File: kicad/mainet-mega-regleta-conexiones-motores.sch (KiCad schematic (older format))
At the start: 38 parts, among them J106 Screw_Terminal_01x02, J107 Conn_01x01_Male, J108 Conn_01x01_Male, J109 Conn_01x01_Male, J110 Conn_01x01_Male, J111 Conn_01x01_Male, J112 Conn_01x01_Male, J113 Conn_01x01_Male, J114 Conn_01x01_Male, J115 Conn_01x01_Male, J116 Conn_01x01_Male, J117 Conn_01x01_Male, J118 Conn_01x01_Male, J119 Conn_01x01_Male, J120 Conn_01x01_Male, J121 Conn_01x01_Male, J122 Conn_01x01_Male, J123 Conn_01x01_Male, J124 Conn_01x01_Male, J125 Conn_01x01_Male, J126 Conn_01x01_Male, J127 Conn_01x01_Male, J93 Regleta de Conexiones, J94 Screw_Terminal_01x15, J95 Conn_01x01_Male, J96 Conn_01x01_Male, J97 Conn_01x01_Male, J98 Screw_Terminal_01x02, M1 Upper Clutch, M2 Lower Clutch 1, M3 Lower Clutch 2, M4 Brake, M5 Upper Clutch Fan, M6 Lower Clutch 1 Fan, M7 Lower Clutch 2 Fan, M8 Brake Fan

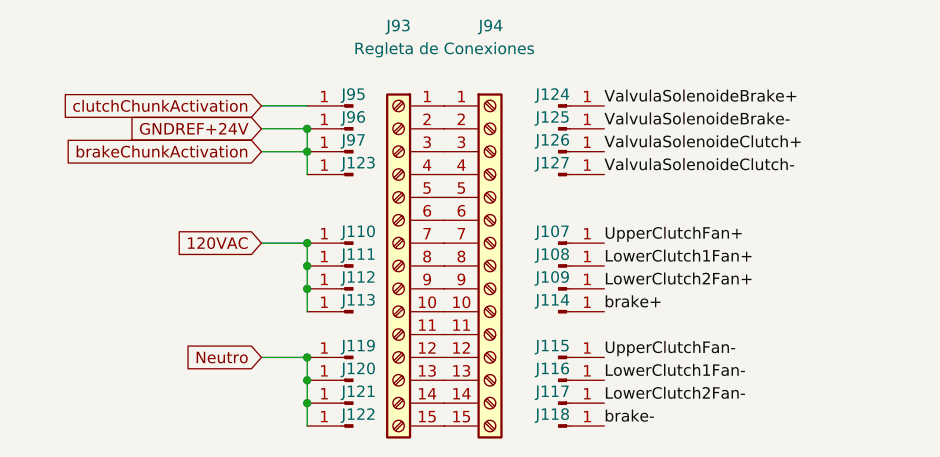
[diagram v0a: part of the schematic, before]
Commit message: KICAD: Agregar conexiones de la Guía de banda regleta de conexiones
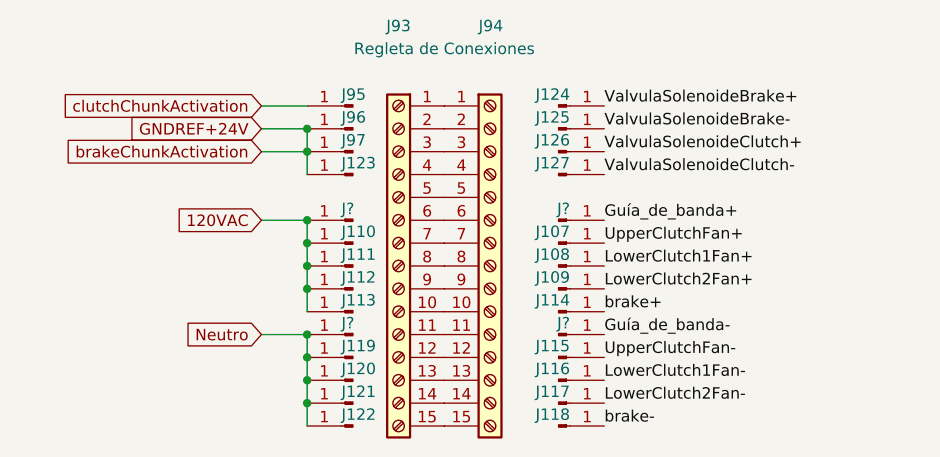
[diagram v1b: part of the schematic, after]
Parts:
- added J? (x4): Conn_01x01_Male, symbol Connector:Conn_01x01_Male
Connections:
- net 120VAC: now also J?.1 (Pin_1)
- net Neutro: now also J?.1 (Pin_1)
- new net Guía_de_banda+: J?.1 (Pin_1)
- new net Guía_de_banda-: J?.1 (Pin_1)
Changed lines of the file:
@@
 Text GLabel 2750 5350 0    50   Input ~ 0
 brakeChunkActivation
-Text GLabel 2750 6250 0    50   Input ~ 0
+Text GLabel 2750 6150 0    50   Input ~ 0
 Neutro
-Text GLabel 2750 5750 0    50   Input ~ 0
+Text GLabel 2750 5650 0    50   Input ~ 0
 120VAC
 $Comp
@@
 	2950 5350 2950 5450
 Wire Wire Line
-	2750 5750 2950 5750
+	2750 5650 2950 5650
 Connection ~ 2950 5750
 Wire Wire Line
-	2750 6250 2950 6250
+	2750 6150 2950 6150
 Connection ~ 2950 6250
 Wire Wire Line
@@
 Text Notes 3350 3500 0    50   ~ 0
 Output-
+$Comp
+L Connector:Conn_01x01_Male J?
+U 1 1 60F7D678
+P 3150 5650
+F 0 "J?" H 3200 5700 50  0000 R CNN
+F 1 "Conn_01x01_Male" H 3122 5583 50  0001 R CNN
+F 2 "" H 3150 5650 50  0001 C CNN
+F 3 "~" H 3150 5650 50  0001 C CNN
+	1    3150 5650
+	-1   0    0    -1
+$EndComp
+$Comp
+L Connector:Conn_01x01_Male J?
+U 1 1 60F7DA90
+P 3150 6150
+F 0 "J?" H 3200 6200 50  0000 R CNN
+F 1 "Conn_01x01_Male" H 3122 6083 50  0001 R CNN
+F 2 "" H 3150 6150 50  0001 C CNN
+F 3 "~" H 3150 6150 50  0001 C CNN
+	1    3150 6150
+	-1   0    0    -1
+$EndComp
+$Comp
+L Connector:Conn_01x01_Male J?
+U 1 1 60F7DEC1
+P 4050 5650
+F 0 "J?" H 4100 5700 50  0000 R CNN
+F 1 "Conn_01x01_Male" H 4022 5583 50  0001 R CNN
+F 2 "" H 4050 5650 50  0001 C CNN
+F 3 "~" H 4050 5650 50  0001 C CNN
+	1    4050 5650
+	1    0    0    -1
+$EndComp
+$Comp
+L Connector:Conn_01x01_Male J?
+U 1 1 60F7E2BC
+P 4050 6150
+F 0 "J?" H 4100 6200 50  0000 R CNN
+F 1 "Conn_01x01_Male" H 4022 6083 50  0001 R CNN
+F 2 "" H 4050 6150 50  0001 C CNN
+F 3 "~" H 4050 6150 50  0001 C CNN
+	1    4050 6150
+	1    0    0    -1
+$EndComp
+Wire Wire Line
+	2950 6150 2950 6250
+Wire Wire Line
+	2950 5650 2950 5750
+Connection ~ 2950 5650
+Connection ~ 2950 6150
+Text Label 4250 5650 0    50   ~ 0
+Guía_de_banda+
+Text Label 4250 6150 0    50   ~ 0
+Guía_de_banda-
 $EndSCHEMATC

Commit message: KICAD: Actualizar .sch regleta de conexiones Agrega conexión para la guía de banda
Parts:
- added J132: Screw_Terminal_01x02, symbol Connector:Screw_Terminal_01x02
- gave numbers to parts that had none: 4
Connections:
- net Guía_de_banda+: now also J132.1 (Pin_1)
- net Guía_de_banda-: now also J132.2 (Pin_2)
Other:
- note added: "120VAC"
- note added: "Guía de banda"
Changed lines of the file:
@@
 Output-
 $Comp
-L Connector:Conn_01x01_Male J?
+L Connector:Conn_01x01_Male J128
 U 1 1 60F7D678
 P 3150 5650
-F 0 "J?" H 3200 5700 50  0000 R CNN
+F 0 "J128" H 3200 5700 50  0000 R CNN
 F 1 "Conn_01x01_Male" H 3122 5583 50  0001 R CNN
 F 2 "" H 3150 5650 50  0001 C CNN
@@
 $EndComp
 $Comp
-L Connector:Conn_01x01_Male J?
+L Connector:Conn_01x01_Male J129
 U 1 1 60F7DA90
 P 3150 6150
-F 0 "J?" H 3200 6200 50  0000 R CNN
+F 0 "J129" H 3200 6200 50  0000 R CNN
 F 1 "Conn_01x01_Male" H 3122 6083 50  0001 R CNN
 F 2 "" H 3150 6150 50  0001 C CNN
@@
 $EndComp
 $Comp
-L Connector:Conn_01x01_Male J?
+L Connector:Conn_01x01_Male J130
 U 1 1 60F7DEC1
 P 4050 5650
-F 0 "J?" H 4100 5700 50  0000 R CNN
+F 0 "J130" H 4100 5700 50  0000 R CNN
 F 1 "Conn_01x01_Male" H 4022 5583 50  0001 R CNN
 F 2 "" H 4050 5650 50  0001 C CNN
@@
 $EndComp
 $Comp
-L Connector:Conn_01x01_Male J?
+L Connector:Conn_01x01_Male J131
 U 1 1 60F7E2BC
 P 4050 6150
-F 0 "J?" H 4100 6200 50  0000 R CNN
+F 0 "J131" H 4100 6200 50  0000 R CNN
 F 1 "Conn_01x01_Male" H 4022 6083 50  0001 R CNN
 F 2 "" H 4050 6150 50  0001 C CNN
@@
 Text Label 4250 6150 0    50   ~ 0
 Guía_de_banda-
+Wire Notes Line
+	6900 5500 6900 6050
+Wire Notes Line
+	6900 6050 8000 6050
+Wire Notes Line
+	8000 6050 8000 5500
+Wire Notes Line
+	8000 5500 6900 5500
+$Comp
+L Connector:Screw_Terminal_01x02 J132
+U 1 1 60FF4B94
+P 8050 5700
+F 0 "J132" H 7968 5825 50  0000 C CNN
+F 1 "Screw_Terminal_01x02" H 7968 5826 50  0001 C CNN
+F 2 "" H 8050 5700 50  0001 C CNN
+F 3 "~" H 8050 5700 50  0001 C CNN
+	1    8050 5700
+	-1   0    0    -1
+$EndComp
+Text Label 8250 5700 0    50   ~ 0
+Guía_de_banda+
+Text Label 8250 5800 0    50   ~ 0
+Guía_de_banda-
+Text Notes 7000 5650 0    50   ~ 0
+Guía de banda
+Text Notes 7000 5750 0    50   ~ 0
+120VAC
 $EndSCHEMATC
